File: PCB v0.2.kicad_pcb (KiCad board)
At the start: 2 copper layers, 77.4 x 97 mm, 60 parts, among them J1 XT60 M (Horizontal), J10 2.54mm 3P, J11 2.54mm 3P, J12 2.54mm 3P, J13 JST-SH 3P, J14 JST-SH 3P, J15 JST-SH 3P, J16 JST-SH 3P, J17 JST-SH 3P, J18 JST-SH 3P, J2 Raspberry Pi 5, J3 Screw 2.54mm 5P, J4 Screw Terminal 5P, J5 Screw Terminal 5P, J6 Screw Terminal 5P, J7 Screw Terminal 5P, J8 Screw Terminal 5P, J9 2.54mm 3P, Q1 NCE1540KA, U1 AMASS_XT30PW-F_1x02_P2.50mm_H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, U1 AMASS_XT30PW-M_1x02_P2.50mm_H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, U2 AMASS_XT30PW-F_1x02_P2.50mm_H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, U2 AMASS_XT30PW-M_1x02_P2.50mm_H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

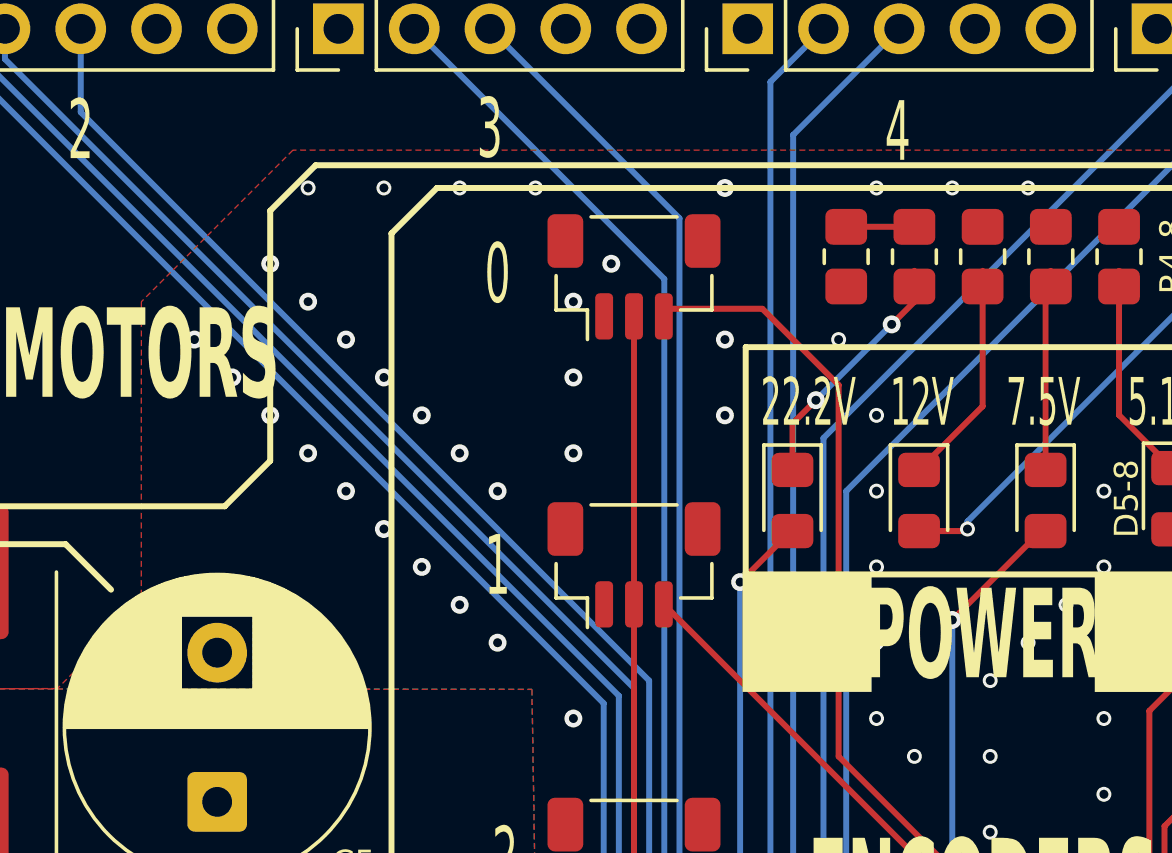
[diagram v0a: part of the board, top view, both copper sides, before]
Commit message: Improved GND return path for BLDC motors
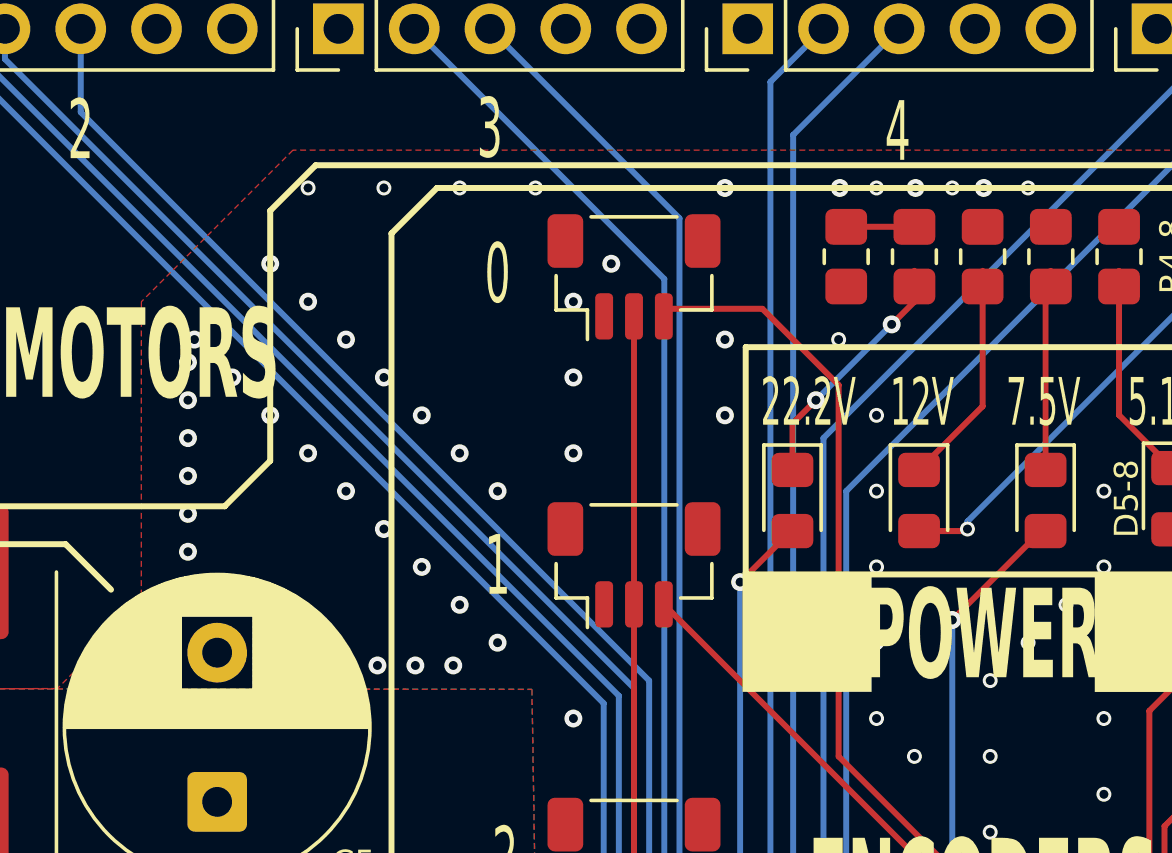
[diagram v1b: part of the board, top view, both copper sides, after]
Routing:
- net GND: vias 331 -> 347
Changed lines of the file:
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@@
+	)
+	(via
+		(at 135.89 62.23)
+		(size 0.6)
+		(drill 0.3)
+		(layers "F.Cu" "B.Cu")
+		(free yes)
+		(net "GND")
 	)
 	(via
@@
 	)
 	(via
+		(at 135.89 63.5)
+		(size 0.6)
+		(drill 0.3)
+		(layers "F.Cu" "B.Cu")
+		(free yes)
+		(net "GND")
+	)
+	(via
 		(at 158.966 75.438)
 		(size 0.5)
@@
 	)
 	(via
+		(at 143.51 68.58)
+		(size 0.6)
+		(drill 0.3)
+		(layers "F.Cu" "B.Cu")
+		(free yes)
+		(net "GND")
+	)
+	(via
 		(at 179.286 55.118)
 		(size 0.5)
@@
 	)
 	(via
+		(at 135.89 58.42)
+		(size 0.6)
+		(drill 0.3)
+		(layers "F.Cu" "B.Cu")
+		(free yes)
+		(net "GND")
+	)
+	(via
+		(at 157.734 52.578)
+		(size 0.6)
+		(drill 0.3)
+		(layers "F.Cu" "B.Cu")
+		(free yes)
+		(net "GND")
+	)
+	(via
 		(at 122.136 136.398)
 		(size 0.6)
@@
 	)
 	(via
+		(at 160.274 52.578)
+		(size 0.6)
+		(drill 0.3)
+		(layers "F.Cu" "B.Cu")
+		(free yes)
+		(net "GND")
+	)
+	(via
 		(at 165.316 86.868)
 		(size 0.5)
@@
 	)
 	(via
+		(at 140.97 68.58)
+		(size 0.6)
+		(drill 0.3)
+		(layers "F.Cu" "B.Cu")
+		(free yes)
+		(net "GND")
+	)
+	(via
 		(at 158.966 67.818)
 		(size 0.5)
@@
 	)
 	(via
+		(at 144.78 68.58)
+		(size 0.6)
+		(drill 0.3)
+		(layers "F.Cu" "B.Cu")
+		(free yes)
+		(net "GND")
+	)
+	(via
 		(at 136.689995 120.366272)
 		(size 0.6)
@@
 	)
 	(via
+		(at 135.89 60.96)
+		(size 0.6)
+		(drill 0.3)
+		(layers "F.Cu" "B.Cu")
+		(free yes)
+		(net "GND")
+	)
+	(via
 		(at 120.866 137.668)
 		(size 0.6)
@@
 	)
 	(via
+		(at 138.43 68.58)
+		(size 0.6)
+		(drill 0.3)
+		(layers "F.Cu" "B.Cu")
+		(free yes)
+		(net "GND")
+	)
+	(via
 		(at 160.236 118.618)
 		(size 0.6)
@@
 	)
 	(via
+		(at 162.56 52.578)
+		(size 0.6)
+		(drill 0.3)
+		(layers "F.Cu" "B.Cu")
+		(free yes)
+		(net "GND")
+	)
+	(via
 		(at 132.296 121.158)
 		(size 0.6)
@@
 	)
 	(via
+		(at 135.89 59.69)
+		(size 0.6)
+		(drill 0.3)
+		(layers "F.Cu" "B.Cu")
+		(free yes)
+		(net "GND")
+	)
+	(via
 		(at 120.866 130.048)
 		(size 0.6)
@@
 	)
 	(via
+		(at 139.7 68.58)
+		(size 0.6)
+		(drill 0.3)
+		(layers "F.Cu" "B.Cu")
+		(free yes)
+		(net "GND")
+	)
+	(via
 		(at 167.856 136.398)
 		(size 0.6)
@@
 	)
 	(via
+		(at 135.89 64.77)
+		(size 0.6)
+		(drill 0.3)
+		(layers "F.Cu" "B.Cu")
+		(free yes)
+		(net "GND")
+	)
+	(via
 		(at 148.806 137.668)
 		(size 0.6)
@@
 		(size 0.6)
 		(drill 0.3)
+		(layers "F.Cu" "B.Cu")
+		(free yes)
+		(net "GND")
+	)
+	(via
+		(at 142.24 68.58)
+		(size 0.6)
+		(drill 0.3)
+		(layers "F.Cu" "B.Cu")
+		(free yes)
+		(net "GND")
+	)
+	(via
+		(at 135.89 66.04)
+		(size 0.6)
+		(drill 0.3)

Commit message: Replaced DC/DC symbol in schematic with appropriate XT30 connectors, fixed XT60 polarity
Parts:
- removed U1, U2: AMASS_XT30PW-F_1x02_P2.50mm_Horizontal, Connector_AMASS:AMASS_XT30PW-F_1x02_P2.50mm_Horizontal
- removed U1, U2: AMASS_XT30PW-M_1x02_P2.50mm_Horizontal, Connector_AMASS:AMASS_XT30PW-M_1x02_P2.50mm_Horizontal
- added J3: XT30-F, Connector_AMASS:AMASS_XT30PW-F_1x02_P2.50mm_Horizontal, F.Cu at (117.4, 88.4)
- added J4: XT30-M, Connector_AMASS:AMASS_XT30PW-M_1x02_P2.50mm_Horizontal, F.Cu at (122.5, 68.5)
- added J5: XT30-F, Connector_AMASS:AMASS_XT30PW-F_1x02_P2.50mm_Horizontal, F.Cu at (117.4, 102.8)
- added J6: XT30-M, Connector_AMASS:AMASS_XT30PW-M_1x02_P2.50mm_Horizontal, F.Cu at (141.0, 129.5)
- J1: value XT60 M (Horizontal) -> XT60-M
- J10: renamed from J6; value Screw Terminal 5P -> Screw 2.54mm 5P
- J11: renamed from J7; value Screw Terminal 5P -> Screw 2.54mm 5P
- J12: renamed from J8; value Screw Terminal 5P -> Screw 2.54mm 5P
- J8: renamed from J4; value Screw Terminal 5P -> Screw 2.54mm 5P
- J9: renamed from J5; value Screw Terminal 5P -> Screw 2.54mm 5P
- moved F1 12.9 mm to (115.3, 119.1), turned to 0 degrees
- moved R4 1.04 mm to (160.5, 55.9)
- moved R5 1.04 mm to (158.2, 55.9)
- moved R6 1.04 mm to (162.8, 55.9)
- moved R7 1.04 mm to (165.1, 55.9)
- moved R8 1.04 mm to (167.4, 55.9)
- moved J1 0.29 mm to (123.2, 126.5)
- renumbered J9 to J13, J10 to J14, J11 to J15, J12 to J16, J13 to J17, J14 to J18, J15 to J19, J16 to J20, J17 to J21, J18 to J22, J3 to J7
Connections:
- F1 pad 1: Net-(J1-Pin_1) -> Net-(J1-Pin_2)
- J1 pad 1: Net-(J1-Pin_1) -> GND
- J1 pad 2: GND -> Net-(J1-Pin_2)
- J17 pad MP: (no net) -> GND
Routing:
- net /ENC_0: track 81.7 -> 79.6 mm
- net Net-(D8-K): track 7.35 -> 5.70 mm
- net Net-(D7-K): track 6.74 -> 5.34 mm
- net Net-(D5-K): track 8.36 -> 6.96 mm, vias 2 -> 0
- net Net-(D6-K): track 7.55 -> 6.15 mm
- net +BATT: track 165.7 -> 167.0 mm
- net Net-(Q1-D): vias 27 -> 0
- net GND: vias 347 -> 361
- added copper zone on B.Cu, net Net-(J1-Pin_2)
- added copper zone on F.Cu, net Net-(J1-Pin_2)
- removed copper zone on B.Cu, net Net-(J1-Pin_1)
- removed copper zone on F.Cu, net Net-(J1-Pin_1)
